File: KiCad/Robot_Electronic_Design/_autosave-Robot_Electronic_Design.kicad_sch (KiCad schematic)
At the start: 3 parts, among them J1 Conn_01x19_Female, J2 Conn_01x19_Female, U1 L298N

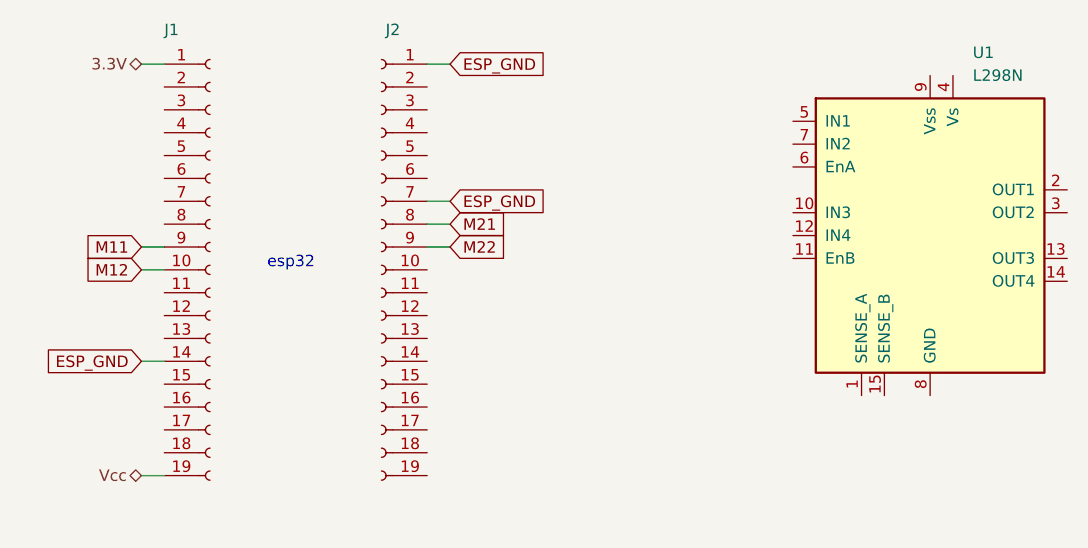
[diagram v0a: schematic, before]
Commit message: chore: Create Arduino Project
- HTML add to library (html.h, html.cpp)
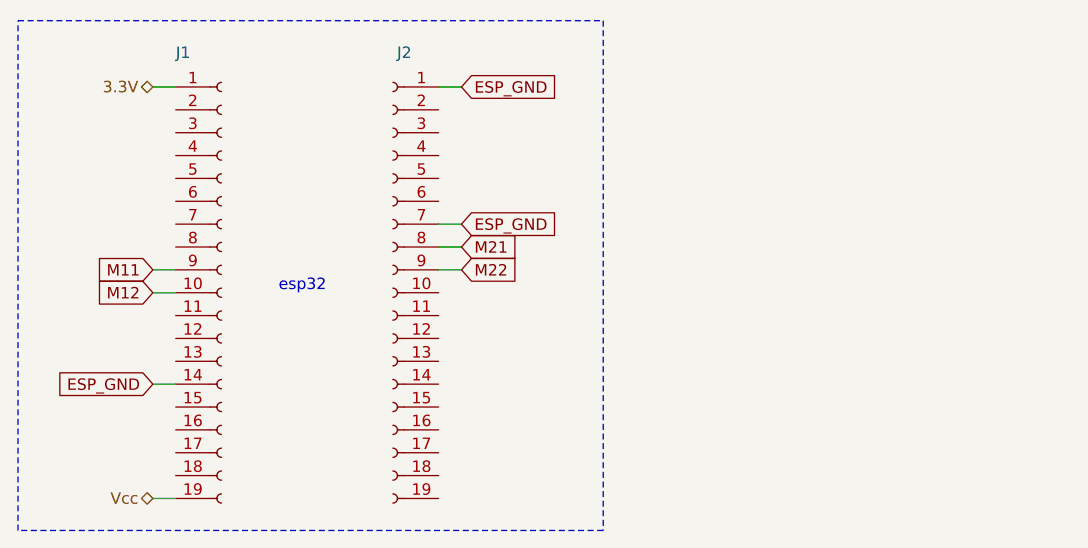
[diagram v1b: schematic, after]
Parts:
- removed U1: L298N, Package_TO_SOT_THT:TO-220-15_P2.54x2.54mm_StaggerOdd_Lead4.58mm_Vertical, symbol Driver_Motor:L298N
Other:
- moved on the sheet: J1, J2
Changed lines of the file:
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@@
 	(wire
 		(pts
-			(xy 67.31 48.26) (xy 69.85 48.26)
-		)
-		(stroke
-			(width 0)
-			(type default)
-		)
-	)
-	(wire
-		(pts
-			(xy 35.56 60.96) (xy 38.1 60.96)
-		)
-		(stroke
-			(width 0)
-			(type default)
-		)
-	)
-	(wire
-		(pts
-			(xy 35.56 48.26) (xy 38.1 48.26)
-		)
-		(stroke
-			(width 0)
-			(type default)
-		)
-	)
-	(wire
-		(pts
-			(xy 35.56 27.94) (xy 38.1 27.94)
-		)
-		(stroke
-			(width 0)
-			(type default)
-		)
-	)
-	(wire
-		(pts
-			(xy 35.56 50.8) (xy 38.1 50.8)
-		)
-		(stroke
-			(width 0)
-			(type default)
-		)
-	)
-	(wire
-		(pts
-			(xy 67.31 27.94) (xy 69.85 27.94)
-		)
-		(stroke
-			(width 0)
-			(type default)
-		)
-	)
-	(wire
-		(pts
-			(xy 67.31 45.72) (xy 69.85 45.72)
-		)
-		(stroke
-			(width 0)
-			(type default)
-		)
-	)
-	(wire
-		(pts
-			(xy 35.56 73.66) (xy 38.1 73.66)
-		)
-		(stroke
-			(width 0)
-			(type default)
-		)
-	)
-	(wire
-		(pts
-			(xy 67.31 43.18) (xy 69.85 43.18)
-		)
-		(stroke
-			(width 0)
-			(type default)
+			(xy 68.58 50.8) (xy 71.12 50.8)
+		)
+		(stroke
+			(width 0)
+			(type default)
+		)
+	)
+	(wire
+		(pts
+			(xy 36.83 63.5) (xy 39.37 63.5)
+		)
+		(stroke
+			(width 0)
+			(type default)
+		)
+	)
+	(wire
+		(pts
+			(xy 36.83 50.8) (xy 39.37 50.8)
+		)
+		(stroke
+			(width 0)
+			(type default)
+		)
+	)
+	(wire
+		(pts
+			(xy 36.83 30.48) (xy 39.37 30.48)
+		)
+		(stroke
+			(width 0)
+			(type default)
+		)
+	)
+	(wire
+		(pts
+			(xy 36.83 53.34) (xy 39.37 53.34)
+		)
+		(stroke
+			(width 0)
+			(type default)
+		)
+	)
+	(wire
+		(pts
+			(xy 68.58 30.48) (xy 71.12 30.48)
+		)
+		(stroke
+			(width 0)
+			(type default)
+		)
+	)
+	(wire
+		(pts
+			(xy 68.58 48.26) (xy 71.12 48.26)
+		)
+		(stroke
+			(width 0)
+			(type default)
+		)
+	)
+	(wire
+		(pts
+			(xy 36.83 76.2) (xy 39.37 76.2)
+		)
+		(stroke
+			(width 0)
+			(type default)
+		)
+	)
+	(wire
+		(pts
+			(xy 68.58 45.72) (xy 71.12 45.72)
+		)
+		(stroke
+			(width 0)
+			(type default)
+		)
+	)
+	(rectangle
+		(start 21.844 23.114)
+		(end 86.868 79.756)
+		(stroke
+			(width 0)
+			(type dash)
+		)
+		(fill
+			(type none)
 		)
 	)
 	(text "esp32"
 		(exclude_from_sim no)
-		(at 49.53 50.8 0)
+		(at 50.8 53.34 0)
 		(effects
 			(font
@@
 	(global_label "ESP_GND"
 		(shape input)
-		(at 69.85 27.94 0)
+		(at 71.12 30.48 0)
 		(fields_autoplaced yes)
 		(effects
@@
 		)
 		(property "Intersheetrefs" "${INTERSHEET_REFS}"
-			(at 80.7298 28.0194 0)
+			(at 81.9998 30.5594 0)
 			(effects
 				(font
@@
 	(global_label "M21"
 		(shape input)
-		(at 69.85 45.72 0)
+		(at 71.12 48.26 0)
 		(fields_autoplaced yes)
 		(effects
@@
 		)
 		(property "Intersheetrefs" "${INTERSHEET_REFS}"
-			(at 76.1336 45.7994 0)
+			(at 77.4036 48.3394 0)
 			(effects
 				(font
@@
 	(global_label "ESP_GND"
 		(shape input)
-		(at 69.85 43.18 0)
+		(at 71.12 45.72 0)
 		(fields_autoplaced yes)
 		(effects
@@
 		)
 		(property "Intersheetrefs" "${INTERSHEET_REFS}"
-			(at 80.7298 43.2594 0)
+			(at 81.9998 45.7994 0)
 			(effects
 				(font
@@
 	(global_label "M11"
 		(shape input)
-		(at 35.56 48.26 180)
+		(at 36.83 50.8 180)
 		(fields_autoplaced yes)
 		(effects
@@
 		)
 		(property "Intersheetrefs" "${INTERSHEET_REFS}"
-			(at 29.2764 48.1806 0)
+			(at 30.5464 50.7206 0)
 			(effects
 				(font
@@
 	(global_label "M12"
 		(shape input)
-		(at 35.56 50.8 180)
+		(at 36.83 53.34 180)
 		(fields_autoplaced yes)
 		(effects
@@
 		)
 		(property "Intersheetrefs" "${INTERSHEET_REFS}"
-			(at 29.2764 50.8794 0)
+			(at 30.5464 53.4194 0)
 			(effects
 				(font
@@
 	(global_label "ESP_GND"
 		(shape input)
-		(at 35.56 60.96 180)
+		(at 36.83 63.5 180)
 		(fields_autoplaced yes)
 		(effects
@@
 		)
 		(property "Intersheetrefs" "${INTERSHEET_REFS}"
-			(at 24.6802 60.8806 0)
+			(at 25.9502 63.4206 0)
 			(effects
 				(font
@@
 	(global_label "M22"
 		(shape input)
-		(at 69.85 48.26 0)
+		(at 71.12 50.8 0)
 		(fields_autoplaced yes)
 		(effects
@@
 		)
 		(property "Intersheetrefs" "${INTERSHEET_REFS}"
-			(at 76.1336 48.1806 0)
+			(at 77.4036 50.7206 0)
 			(effects
 				(font
@@
 	(hierarchical_label "3.3V"
 		(shape bidirectional)
-		(at 35.56 27.94 180)
+		(at 36.83 30.48 180)
 		(fields_autoplaced yes)
 		(effects
@@
 	(hierarchical_label "Vcc"
 		(shape bidirectional)
-		(at 35.56 73.66 180)
+		(at 36.83 76.2 180)
 		(fields_autoplaced yes)
 		(effects
@@
 			)
 			(justify right)
-		)
-	)
-	(symbol
-		(lib_id "Driver_Motor:L298N")
-		(at 123.19 46.99 0)
-		(unit 1)
-		(exclude_from_sim no)
-		(in_bom yes)
-		(on_board yes)
-		(dnp no)
-		(fields_autoplaced yes)
-		(property "Reference" "U1"
-			(at 127.9241 26.67 0)
-			(effects
-				(font
-					(size 1.27 1.27)
-				)
-				(justify left)
-			)
-		)
-		(property "Value" "L298N"
-			(at 127.9241 29.21 0)
-			(effects
-				(font
-					(size 1.27 1.27)
-				)
-				(justify left)
-			)
-		)
-		(property "Footprint" "Package_TO_SOT_THT:TO-220-15_P2.54x2.54mm_StaggerOdd_Lead4.58mm_Vertical"
-			(at 124.46 63.5 0)
-			(effects
-				(font
-					(size 1.27 1.27)
-				)
-				(justify left)
-				(hide yes)
-			)
-		)
-		(property "Datasheet" "http://www.st.com/st-web-ui/static/active/en/resource/technical/document/datasheet/CD00000240.pdf"
-			(at 127 40.64 0)
-			(effects
-				(font
-					(size 1.27 1.27)
-				)
-				(hide yes)
-			)
-		)
-		(property "Description" "Dual full bridge motor driver, up to 46V, 4A, Multiwatt15-V"
-			(at 123.19 46.99 0)
-			(effects
-				(font
-					(size 1.27 1.27)
-				)
-				(hide yes)
-			)
-		)
-		(pin "2"
-		)
-		(pin "10"
-		)
-		(pin "12"
-		)
-		(pin "11"
-		)
-		(pin "3"
-		)
-		(pin "4"
-		)
-		(pin "5"
-		)
-		(pin "8"
-		)
-		(pin "13"
-		)
-		(pin "9"
-		)
-		(pin "1"
-		)
-		(pin "15"
-		)
-		(pin "6"
-		)
-		(pin "7"
-		)
-		(pin "14"
-		)
-		(instances
-			(project ""
-				(path "/67a23c6f-cb01-457f-a901-c3be1e74a6f5"
-					(reference "U1")
-					(unit 1)
-				)
-			)
 		)
 	)
 	(symbol
 		(lib_id "Connector:Conn_01x19_Female")
-		(at 62.23 50.8 0)
+		(at 63.5 53.34 0)
 		(mirror y)
 		(unit 1)
@@
 		(dnp no)
 		(property "Reference" "J2"
-			(at 63.5 24.13 0)
+			(at 64.77 26.67 0)
 			(effects
 				(font
@@
 		)
 		(property "Value" "Conn_01x19_Female"
-			(at 62.865 25.4 0)
+			(at 64.135 27.94 0)
 			(effects
 				(font
@@
 		)
 		(property "Footprint" "Connector_PinSocket_2.54mm:PinSocket_1x19_P2.54mm_Vertical"
-			(at 62.23 50.8 0)
+			(at 63.5 53.34 0)
 			(effects
 				(font
@@
 		)
 		(property "Datasheet" "~"
-			(at 62.23 50.8 0)
+			(at 63.5 53.34 0)
 			(effects
 				(font
@@
 		)
 		(property "Description" ""
-			(at 62.23 50.8 0)
+			(at 63.5 53.34 0)
 			(effects
 				(font
@@
 	(symbol
 		(lib_id "Connector:Conn_01x19_Female")
-		(at 43.18 50.8 0)
+		(at 44.45 53.34 0)
 		(unit 1)
 		(exclude_from_sim no)
@@
 		(dnp no)
 		(property "Reference" "J1"
-			(at 38.1 24.13 0)
+			(at 39.37 26.67 0)
 			(effects
 				(font
@@
 		)
 		(property "Value" "Conn_01x19_Female"
-			(at 31.75 25.4 0)
+			(at 33.02 27.94 0)
 			(effects
 				(font
@@
 		)
 		(property "Footprint" "Connector_PinSocket_2.54mm:PinSocket_1x19_P2.54mm_Vertical"
-			(at 43.18 50.8 0)
+			(at 44.45 53.34 0)
 			(effects
 				(font
@@
 		)
 		(property "Datasheet" "~"
-			(at 43.18 50.8 0)
+			(at 44.45 53.34 0)
 			(effects
 				(font
@@
 		)
 		(property "Description" ""
-			(at 43.18 50.8 0)
-			(effects
-				(font
+			(at 44.45 53.34 0)
+			(effects
+				(font
